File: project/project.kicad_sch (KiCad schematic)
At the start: 22 parts, among them J101 Front, J102 FFC, SW101 SW_DIP_x04, U101 GX101

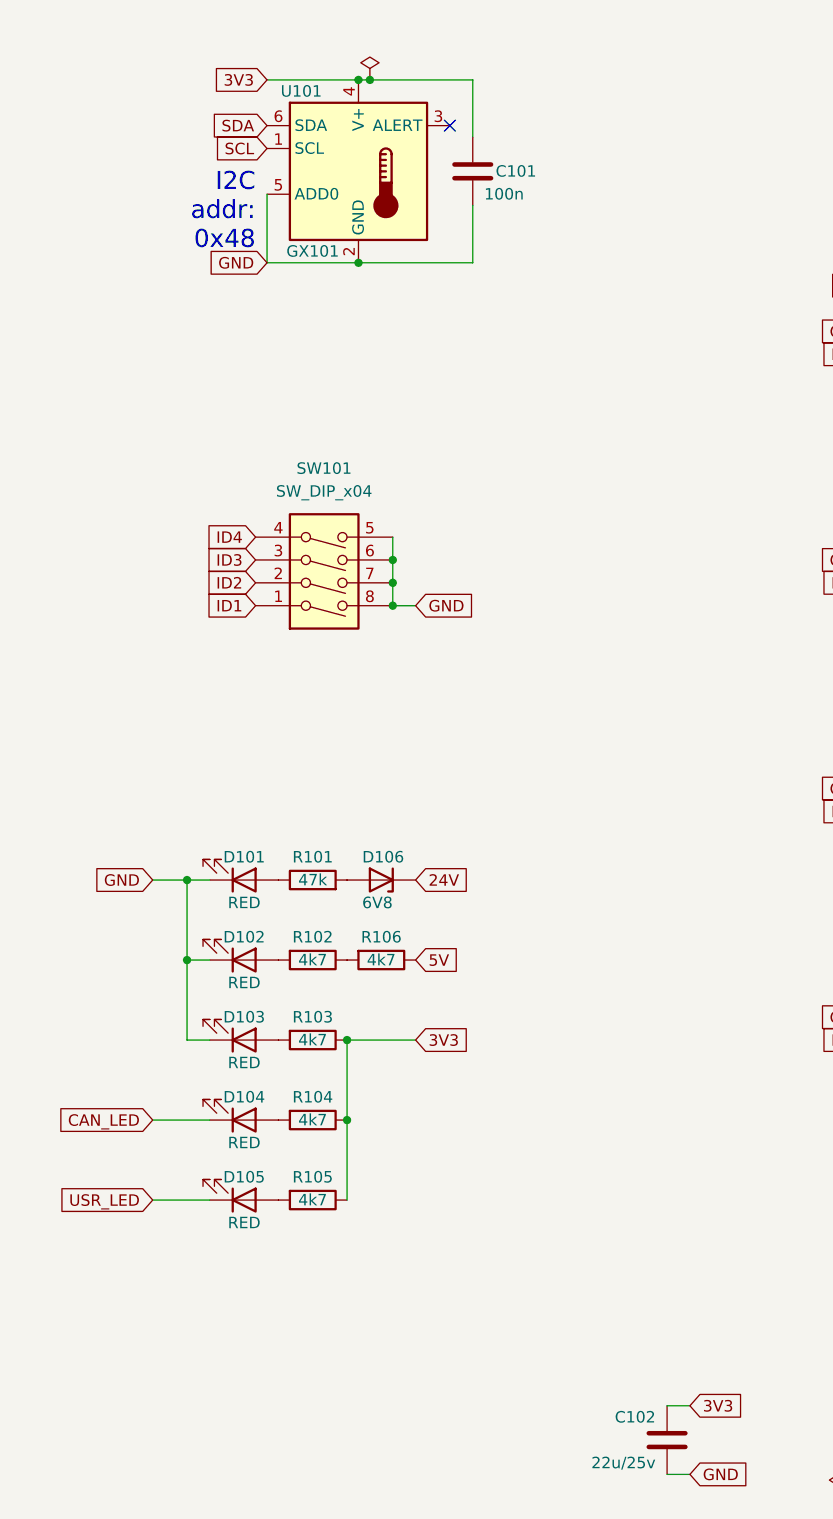
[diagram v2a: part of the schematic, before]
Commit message: parts consolidation and small fixes
* Inverting input LEDs
* Switching to TMP102 as TMP101 is no longer available
* Helping 74HC forget state after power loss
* bumping up version
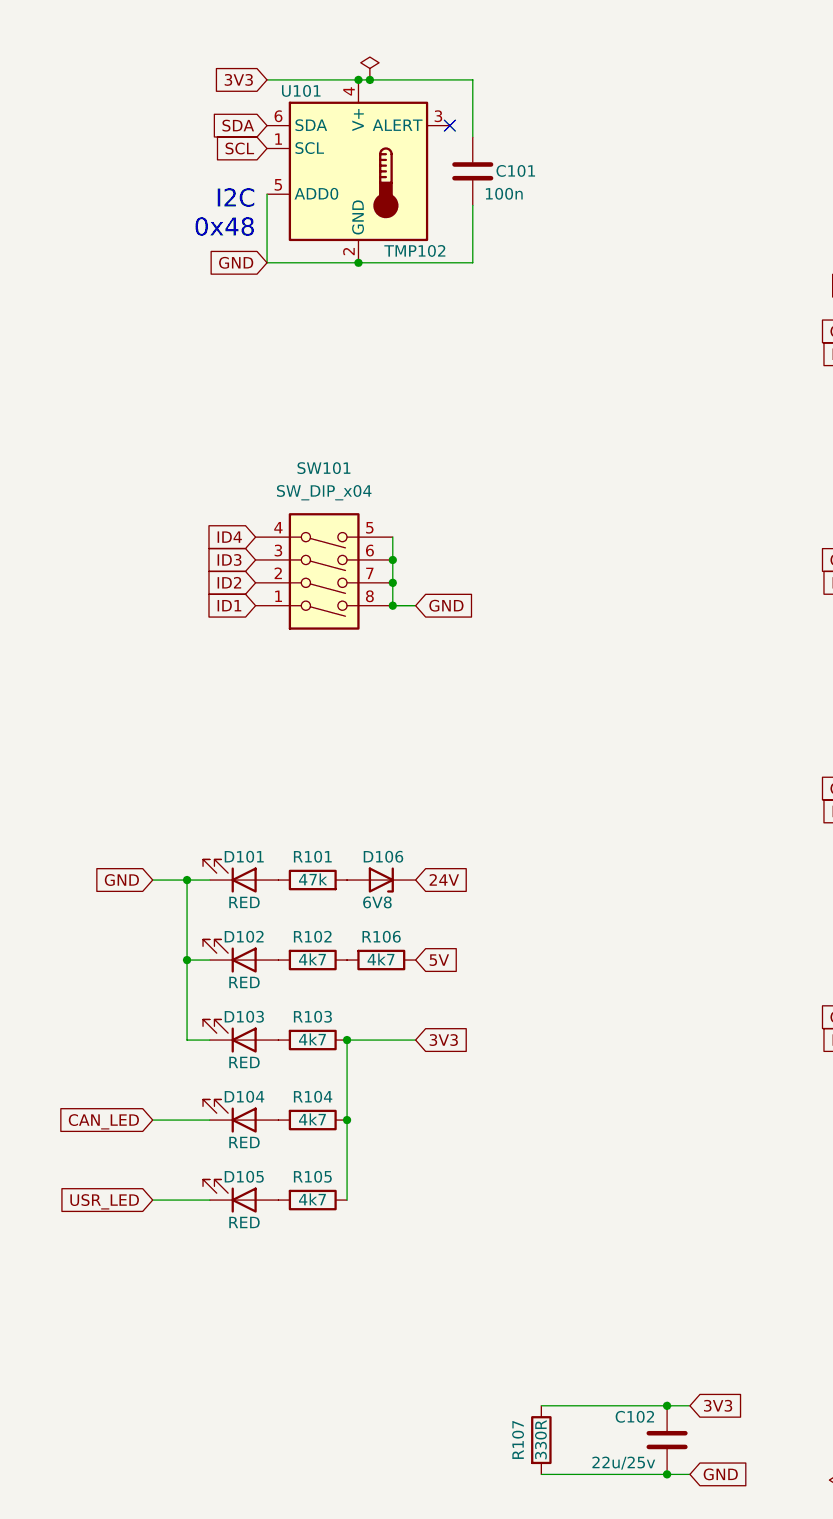
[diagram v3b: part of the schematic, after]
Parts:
- added R107: 330R, Resistor_SMD:R_0402_1005Metric_Pad0.72x0.64mm_HandSolder, symbol Device:R
- U101: value GX101 -> TMP102; footprint Package_TO_SOT_SMD:SOT-23-6 -> -local:SOT-563; lcsc# C5441728 -> C99269
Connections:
- net 3V3: now also R107.1
- net GND: now also R107.2
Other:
- note added: "I2C 0x48"
- note removed: "I2C addr: 0x48"
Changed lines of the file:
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@@
   (title_block
     (title "WormControl-Input32-UIBoard")
-    (date "2026-02-10")
-    (rev "0.1")
+    (date "2026-03-19")
+    (rev "0.2")
     (company "makerspace.lt")
   )
@@
   (junction (at 152.4 196.85) (diameter 0) (color 0 0 0 0)
   )
+  (junction (at 127 194.31) (diameter 0) (color 0 0 0 0)
+  )
   (junction (at 91.44 146.05) (diameter 0) (color 0 0 0 0)
   )
@@
   )
   (junction (at 93.98 39.37) (diameter 0) (color 0 0 0 0)
+  )
+  (junction (at 127 186.69) (diameter 0) (color 0 0 0 0)
   )
   (junction (at 96.52 92.71) (diameter 0) (color 0 0 0 0)
@@
     (stroke (width 0) (type default) (color 0 0 0 0))
   )
+  (wire (pts (xy 113.03 186.69) (xy 127 186.69))
+    (stroke (width 0) (type default) (color 0 0 0 0))
+  )
   (wire (pts (xy 105.41 53.34) (xy 105.41 59.69))
     (stroke (width 0) (type default) (color 0 0 0 0))
@@
     (stroke (width 0) (type default) (color 0 0 0 0))
   )
+  (wire (pts (xy 113.03 194.31) (xy 127 194.31))
+    (stroke (width 0) (type default) (color 0 0 0 0))
+  )
   (wire (pts (xy 105.41 59.69) (xy 92.71 59.69))
     (stroke (width 0) (type default) (color 0 0 0 0))
@@
     (stroke (width 0) (type default) (color 0 0 0 0))
   )
-  (text "I2C\naddr:\n0x48" (at 81.28 58.42 180)
+  (text "I2C\n0x48" (at 81.28 57.15 180)
     (effects (font (size 2 2)) (justify right bottom))
   )
@@
     (in_bom yes) (on_board yes)
     (property "Reference" "U101" (id 0) (at 86.36 40.64 0))
-    (property "Value" "GX101" (id 1) (at 87.63 58.42 0))
-    (property "Footprint" "Package_TO_SOT_SMD:SOT-23-6" (id 2) (at 93.98 58.42 0)
-      (effects (font (size 1.27 1.27)) (justify left) hide)
-    )
-    (property "Datasheet" "https://www.lcsc.com/datasheet/lcsc_datasheet_2409280202_GXCAS-GX101S_C5441728.pdf" (id 3) (at 93.98 60.96 0)
+    (property "Value" "TMP102" (id 1) (at 99.06 58.42 0))
+    (property "Footprint" "-local:SOT-563" (id 2) (at 93.98 58.42 0)
+      (effects (font (size 1.27 1.27)) (justify left) hide)
+    )
+    (property "Datasheet" "https://www.lcsc.com/datasheet/C99269.pdf" (id 3) (at 93.98 60.96 0)
       (effects (font (size 1.27 1.27)) (justify left) hide)
     )
@@
       (effects (font (size 1.27 1.27)) hide)
     )
-    (property "lcsc#" "C5441728" (id 5) (at 92.71 49.53 0)
+    (property "lcsc#" "C99269" (id 5) (at 92.71 49.53 0)
       (effects (font (size 1.27 1.27)) hide)
     )
@@
     )
     (pin "1")
+  )
+  (symbol (lib_id "Device:R") (at 113.03 190.5 0) (unit 1)
+    (in_bom yes) (on_board yes)
+    (property "Reference" "R107" (id 0) (at 110.49 190.5 90))
+    (property "Value" "330R" (id 1) (at 113.03 190.5 90))
+    (property "Footprint" "Resistor_SMD:R_0402_1005Metric_Pad0.72x0.64mm_HandSolder" (id 2) (at 111.252 190.5 90)
+      (effects (font (size 1.27 1.27)) hide)
+    )
+    (property "Datasheet" "~" (id 3) (at 113.03 190.5 0)
+      (effects (font (size 1.27 1.27)) hide)
+    )
+    (property "jlc-part-type" "B" (id 4) (at 113.03 190.5 0)
+      (effects (font (size 1.27 1.27)) hide)
+    )
+    (property "lcsc#" "C25104" (id 5) (at 113.03 190.5 0)
+      (effects (font (size 1.27 1.27)) hide)
+    )
+    (pin "1")
+    (pin "2")
   )
   (sheet (at 152.4 109.22) (size 25.4 17.78)
@@
       (reference "R106") (unit 1) (value "4k7") (footprint "Resistor_SMD:R_0402_1005Metric_Pad0.72x0.64mm_HandSolder")
     )
+    (path "/fe27cc5b-941e-4d85-bc76-fcedcb2e94cb"
+      (reference "R107") (unit 1) (value "330R") (footprint "Resistor_SMD:R_0402_1005Metric_Pad0.72x0.64mm_HandSolder")
+    )
     (path "/e3c417ce-36bc-4032-ad2f-baf14f130df6/1f5217de-3aa4-4634-a7a5-037afe748a8c"
       (reference "R201") (unit 1) (value "330R") (footprint "Resistor_SMD:R_0402_1005Metric_Pad0.72x0.64mm_HandSolder")
@@
     )
     (path "/55cbd1b5-ecb1-4b1b-9a94-3461217e0d3f"
-      (reference "U101") (unit 1) (value "GX101") (footprint "Package_TO_SOT_SMD:SOT-23-6")
+      (reference "U101") (unit 1) (value "TMP102") (footprint "-local:SOT-563")
     )
     (path "/e3c417ce-36bc-4032-ad2f-baf14f130df6/95dcdad2-39b4-4cf4-ba3f-0d1a6d4d30a8"

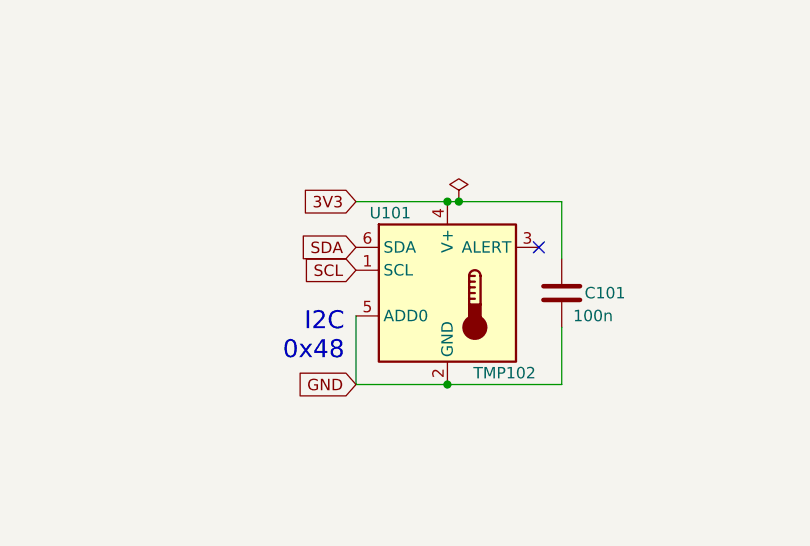
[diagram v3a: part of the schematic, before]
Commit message: fixing tmp102 pinout
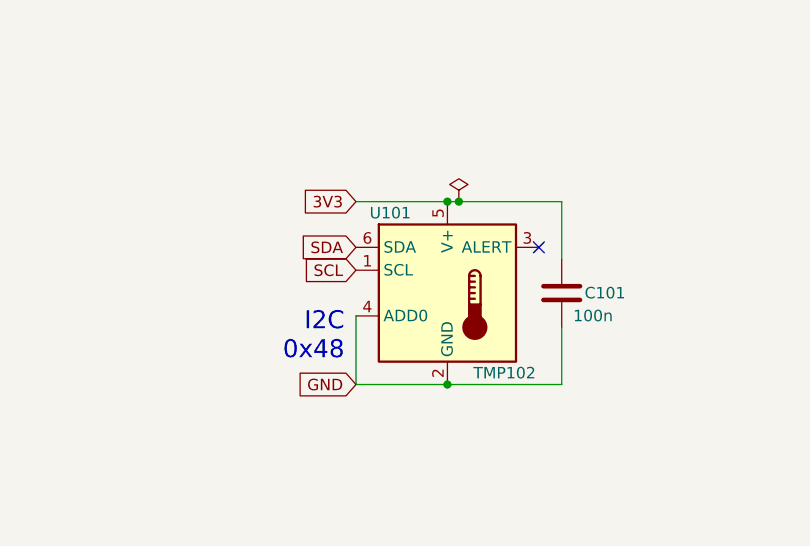
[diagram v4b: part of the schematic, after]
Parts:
- U101: symbol Sensor_Temperature:TMP101 -> Sensor_Temperature:TMP102xxDRL
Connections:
- net 3V3: now also U101.5 (V+); no longer U101.4 (V+)
- net GND: now also U101.4 (ADD0); no longer U101.5 (ADD0)
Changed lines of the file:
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@@
     (pin "2")
   )
-  (symbol (lib_id "Sensor_Temperature:TMP101") (at 92.71 49.53 0) (unit 1)
+  (symbol (lib_id "Sensor_Temperature:TMP102xxDRL") (at 92.71 49.53 0) (unit 1)
     (in_bom yes) (on_board yes)
     (property "Reference" "U101" (id 0) (at 86.36 40.64 0))
@@
       (effects (font (size 1.27 1.27)) (justify left) hide)
     )
-    (property "Datasheet" "https://www.lcsc.com/datasheet/C99269.pdf" (id 3) (at 93.98 60.96 0)
+    (property "Datasheet" "https://www.ti.com/lit/ds/symlink/tmp102.pdf" (id 3) (at 93.98 60.96 0)
       (effects (font (size 1.27 1.27)) (justify left) hide)
     )
